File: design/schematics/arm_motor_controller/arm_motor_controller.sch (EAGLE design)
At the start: 64 parts

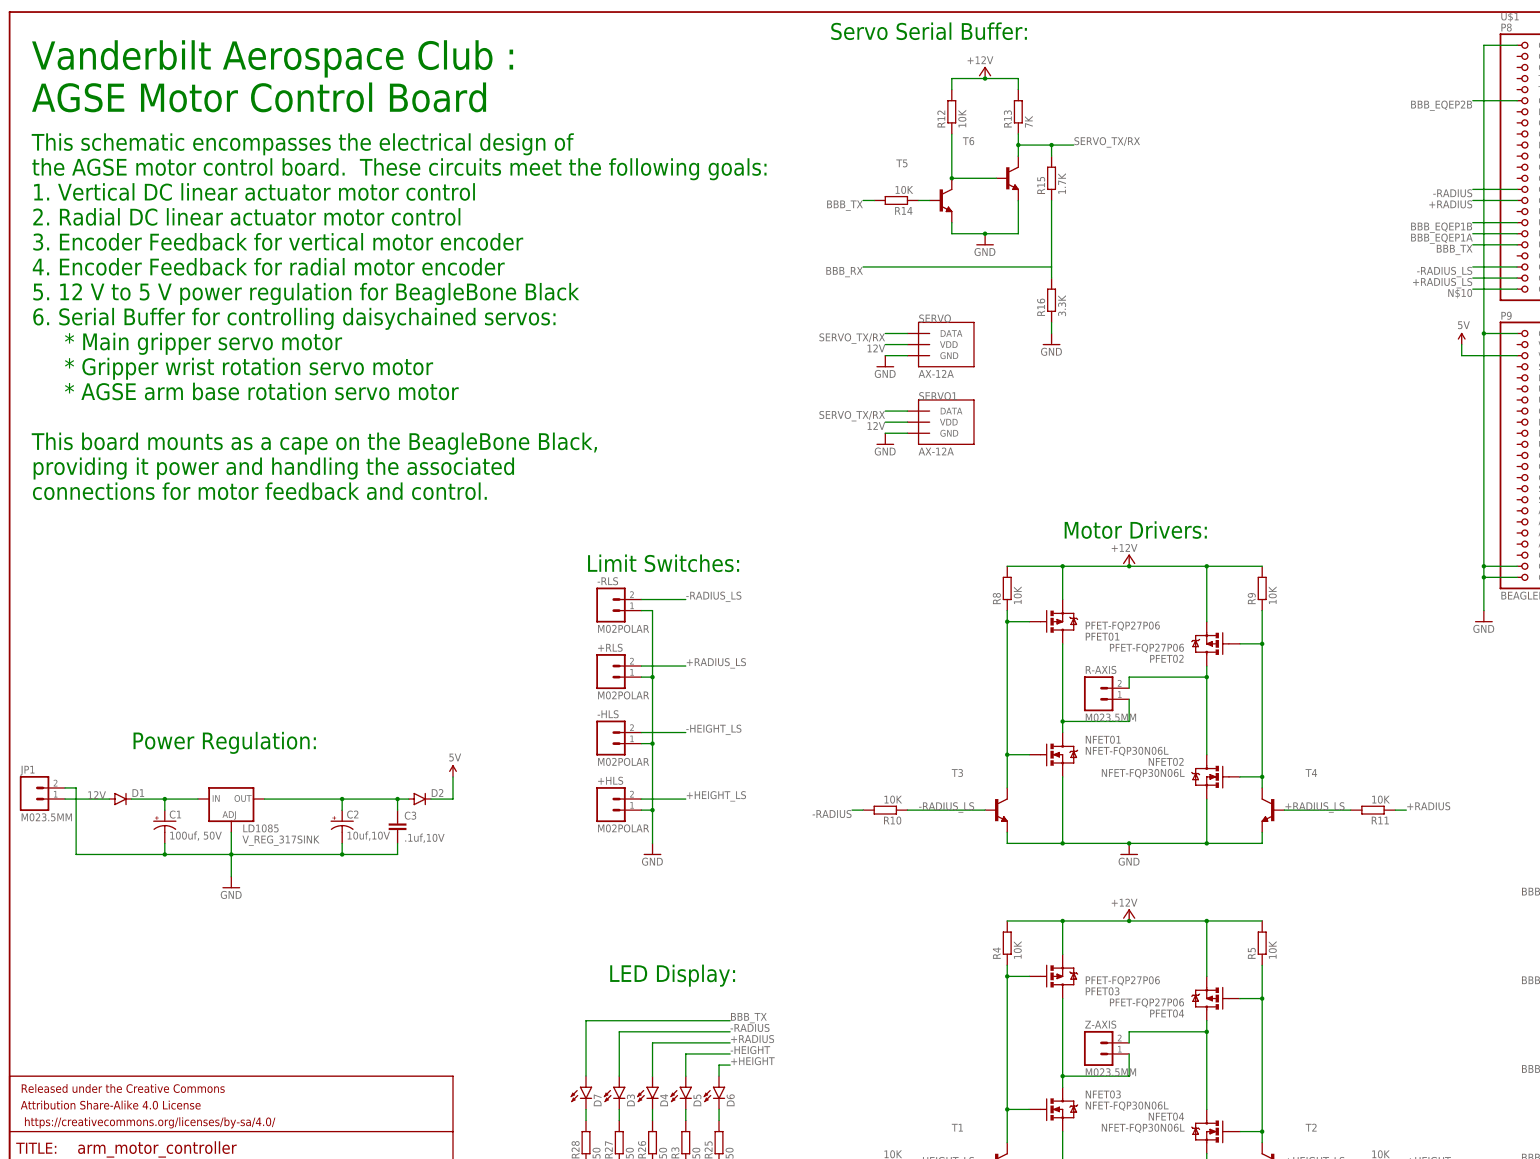
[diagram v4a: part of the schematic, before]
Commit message: updated boards and BoM.  added PTCs, changed to molex connectors, and updated diode and other componenets.
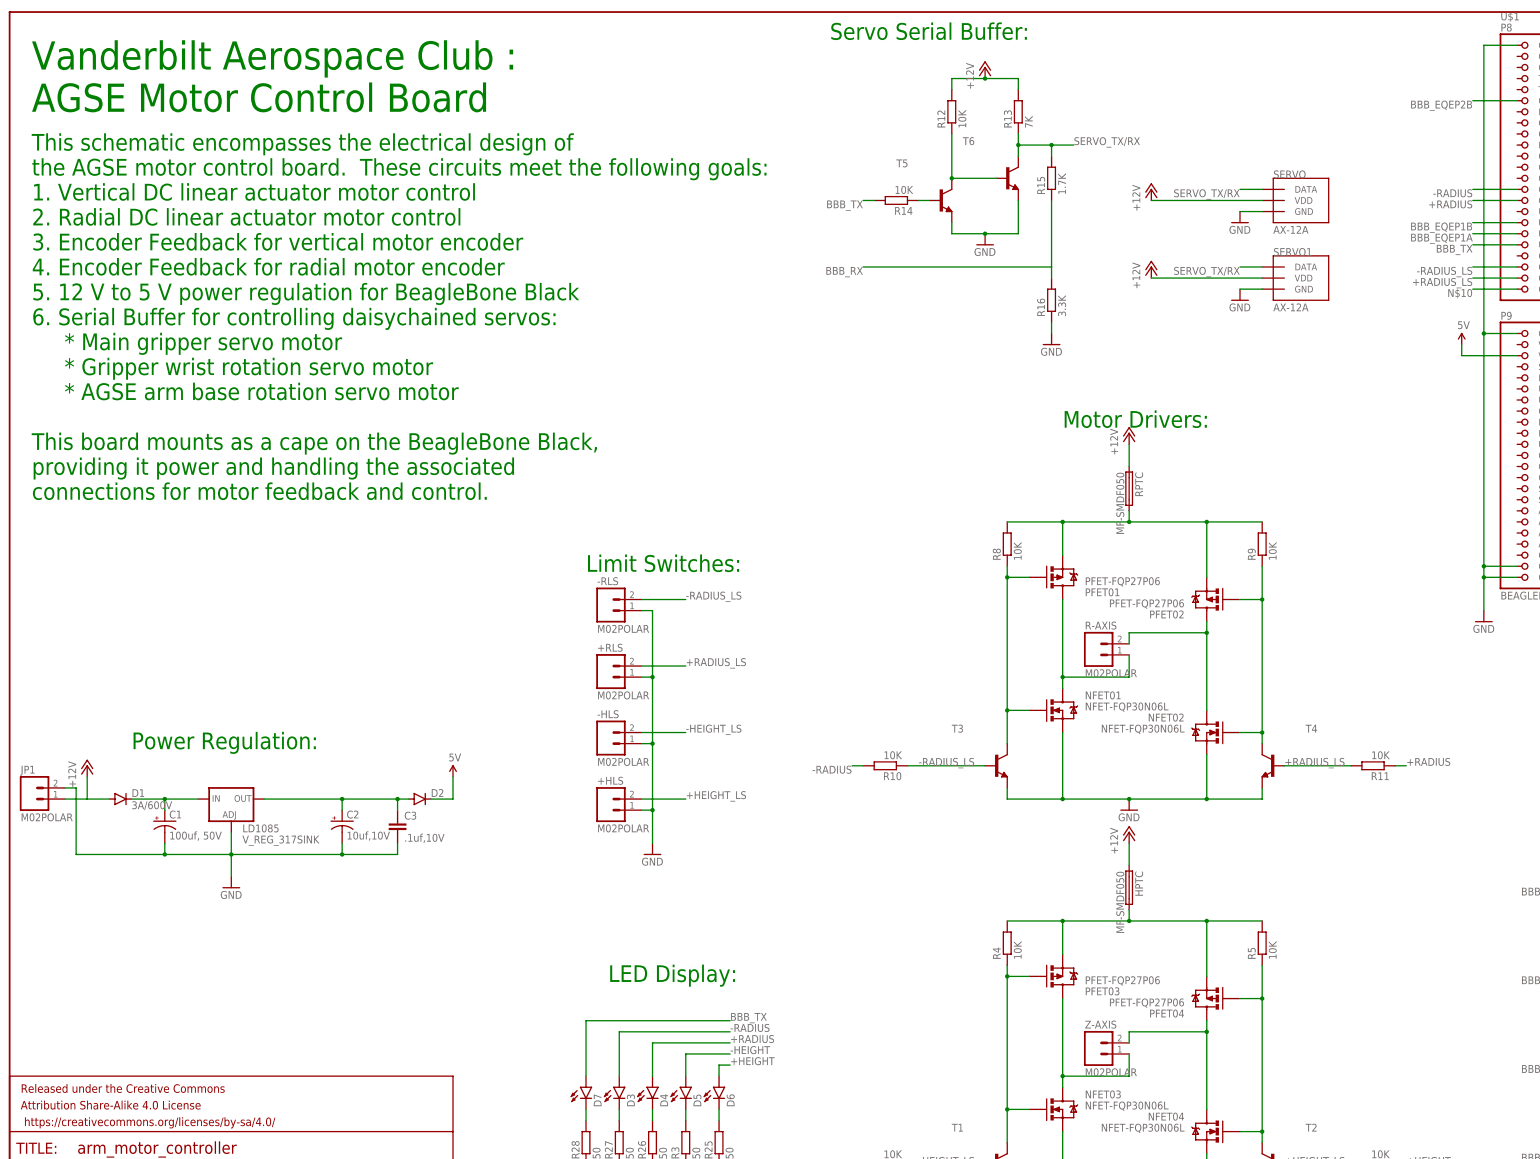
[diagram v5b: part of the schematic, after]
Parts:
- added HPTC, RPTC: MF-SMDF050, fuse:MF-SMDF050
- D1: value (none) -> 3A/600V; device SparkFun-DiscreteSemi:DIODESMA -> SparkFun-DiscreteSemi:DIODEES3J
- JP1, R-AXIS, Z-AXIS: value M023.5MM -> M02POLAR; device SparkFun-Connectors:M023.5MM -> SparkFun-Connectors:M02POLAR
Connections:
- removed net 12V: D1.A, JP1.1, PFET01.S, PFET02.S, PFET03.S, PFET04.S, R12.2, R13.2, R4.2, R5.2, R8.2, R9.2, SERVO.VDD, SERVO1.VDD
- new net +12V: D1.A, HPTC.1, JP1.1, R12.2, R13.2, RPTC.1, SERVO.VDD, SERVO1.VDD
- new net H_VDD: HPTC.2, PFET03.S, PFET04.S, R4.2, R5.2
- new net R_VDD: PFET01.S, PFET02.S, R8.2, R9.2, RPTC.2
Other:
- moved on the sheet: NFET01, NFET02, PFET01, PFET02, R-AXIS, R10, R11, R8, R9, SERVO, SERVO1, T3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
